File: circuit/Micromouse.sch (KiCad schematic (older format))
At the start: 33 parts, among them J1 DBG_CN, J3 TEST_1P, J5 TEST_1P, J6 Conn_01x04, Q2 IRLML6344, SW2 SW_Push, SW3 SW_Push, SW4 SW_Push, U3 STM32F405RGTx, U7 ICM-20602-module

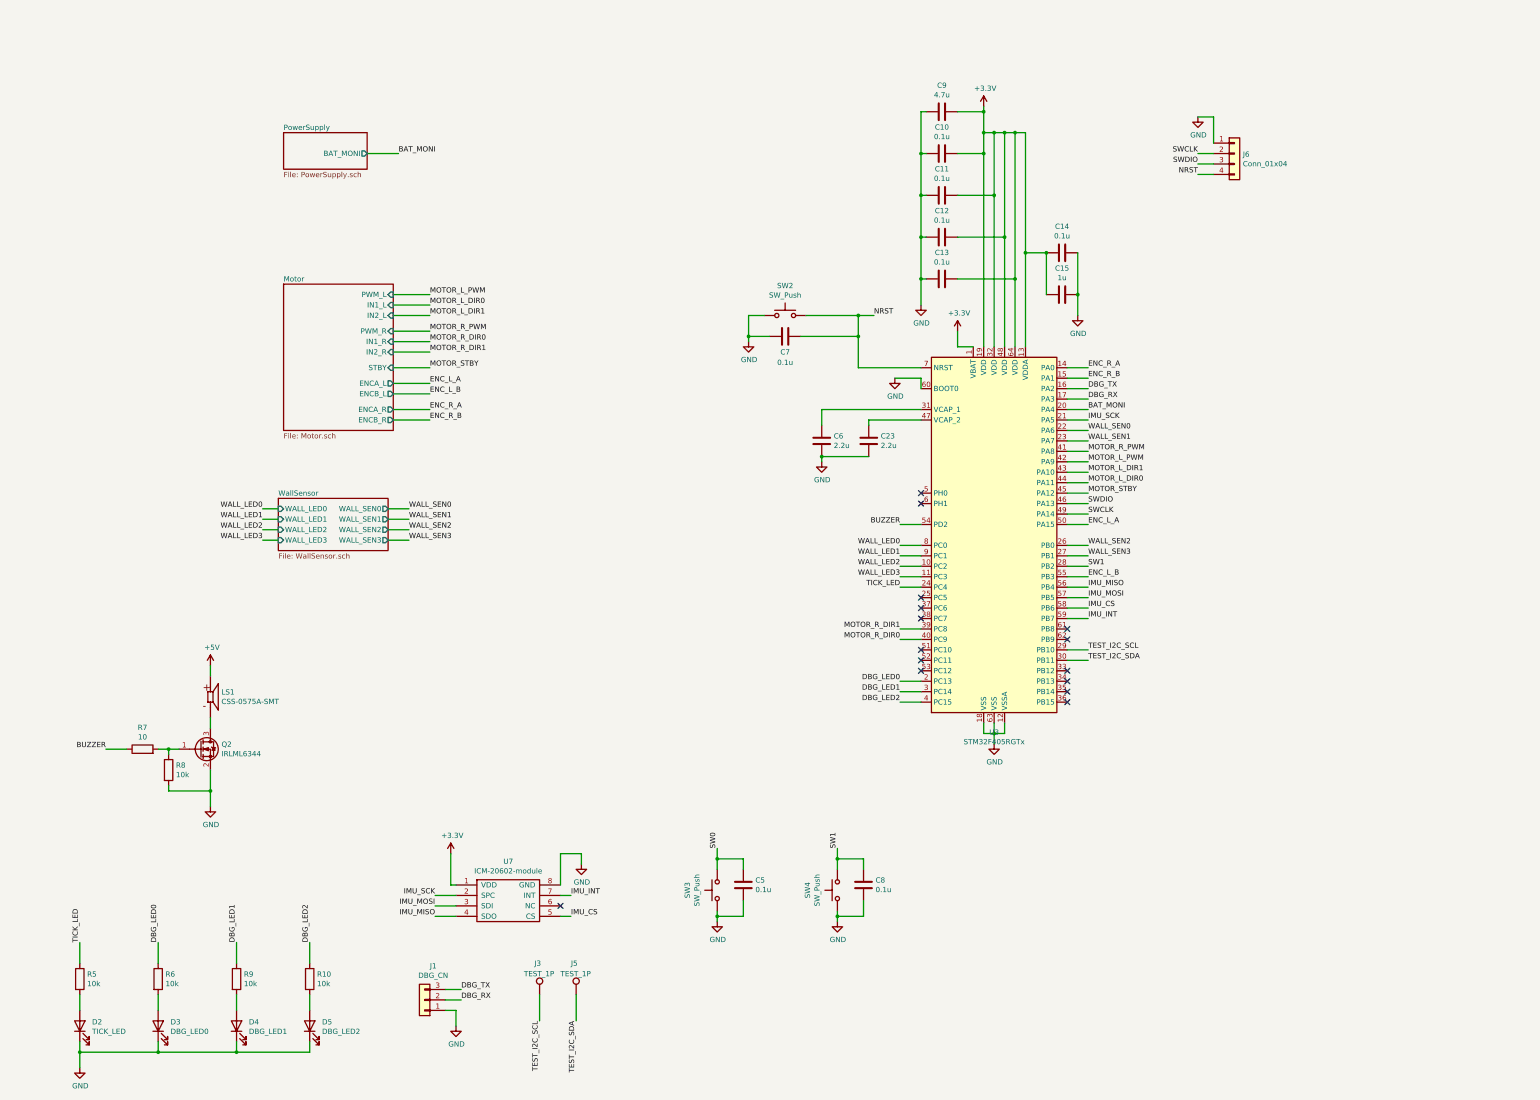
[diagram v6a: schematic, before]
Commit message: 残すはGNDビアとGND分離・・・
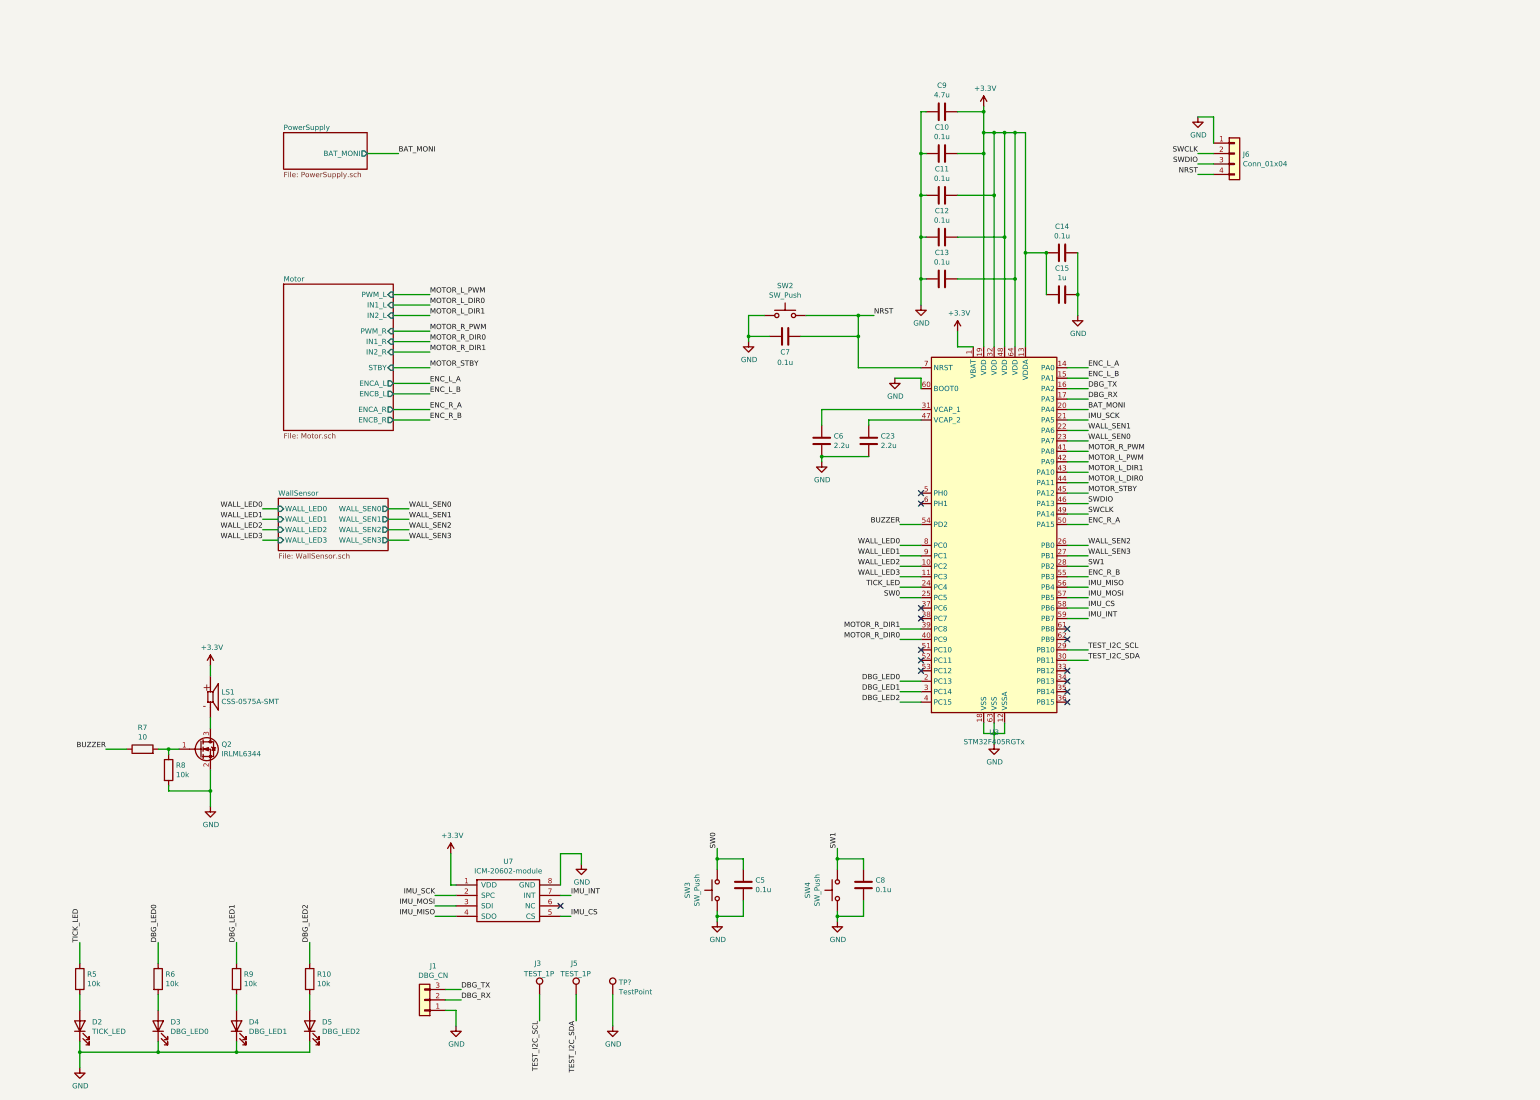
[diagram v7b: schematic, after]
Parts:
- added TP?: TestPoint, symbol Connector:TestPoint
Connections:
- net +5V is gone; now on net +3V3: LS1.1
- net ENC_L_A: now also U3.14 (PA0); no longer U3.50 (PA15)
- net ENC_L_B: now also U3.15 (PA1); no longer U3.55 (PB3)
- net ENC_R_A: now also U3.50 (PA15); no longer U3.14 (PA0)
- net ENC_R_B: now also U3.55 (PB3); no longer U3.15 (PA1)
- net GND: now also TP?.1
- net SW0: now also U3.25 (PC5)
- net WALL_SEN0: now also U3.23 (PA7); no longer U3.22 (PA6)
- net WALL_SEN1: now also U3.22 (PA6); no longer U3.23 (PA7)
- no-connect marks 15 -> 14
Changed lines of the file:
@@
 	10850 3800 11050 3800
 Text Label 11050 3900 0    50   ~ 0
-ENC_R_B
+ENC_L_B
 Wire Wire Line
 	10850 3900 11050 3900
 Text Label 11050 3800 0    50   ~ 0
-ENC_R_A
+ENC_L_A
 Text Label 11050 4000 0    50   ~ 0
 DBG_TX
@@
 	10850 4300 11050 4300
 Text Label 11050 4400 0    50   ~ 0
-WALL_SEN0
+WALL_SEN1
 Wire Wire Line
 	10850 4400 11050 4400
 Text Label 11050 4500 0    50   ~ 0
-WALL_SEN1
+WALL_SEN0
 Wire Wire Line
 	10850 4500 11050 4500
@@
 	10850 5000 11050 5000
 Text Label 11050 5300 0    50   ~ 0
-ENC_L_A
+ENC_R_A
 Wire Wire Line
 	10850 5300 11050 5300
 Text Label 11050 5800 0    50   ~ 0
-ENC_L_B
+ENC_R_B
 Wire Wire Line
 	10850 5800 11050 5800
@@
 NoConn ~ 10850 6400
 NoConn ~ 10850 6300
-NoConn ~ 9450 6000
 Text Label 7500 8400 1    50   ~ 0
 SW0
@@
 $EndComp
 $Comp
-L power:+5V #PWR0128
-U 1 1 5FAB5052
-P 2650 6650
-F 0 "#PWR0128" H 2650 6500 50  0001 C CNN
-F 1 "+5V" H 2665 6823 50  0000 C CNN
-F 2 "" H 2650 6650 50  0001 C CNN
-F 3 "" H 2650 6650 50  0001 C CNN
-	1    2650 6650
-	1    0    0    -1
-$EndComp
-$Comp
 L Connector_Generic:Conn_01x03 J1
 U 1 1 5FA91BF0
@@
 	6000 8850 6100 8850
 NoConn ~ 6000 8950
+$Comp
+L power:+3.3V #PWR0128
+U 1 1 5FCF8981
+P 2650 6650
+F 0 "#PWR0128" H 2650 6500 50  0001 C CNN
+F 1 "+3.3V" H 2665 6823 50  0000 C CNN
+F 2 "" H 2650 6650 50  0001 C CNN
+F 3 "" H 2650 6650 50  0001 C CNN
+	1    2650 6650
+	1    0    0    -1
+$EndComp
+Text Label 9250 6000 2    50   ~ 0
+SW0
+Wire Wire Line
+	9250 6000 9450 6000
+$Comp
+L Connector:TestPoint TP?
+U 1 1 5FFC074B
+P 6500 9800
+F 0 "TP?" H 6558 9918 50  0000 L CNN
+F 1 "TestPoint" H 6558 9827 50  0000 L CNN
+F 2 "" H 6700 9800 50  0001 C CNN
+F 3 "~" H 6700 9800 50  0001 C CNN
+	1    6500 9800
+	1    0    0    -1
+$EndComp
+$Comp
+L power:GND #PWR?
+U 1 1 5FFC282D
+P 6500 10100
+F 0 "#PWR?" H 6500 9850 50  0001 C CNN
+F 1 "GND" H 6505 9927 50  0000 C CNN
+F 2 "" H 6500 10100 50  0001 C CNN
+F 3 "" H 6500 10100 50  0001 C CNN
+	1    6500 10100
+	1    0    0    -1
+$EndComp
+Wire Wire Line
+	6500 9800 6500 10100
 $EndSCHEMATC

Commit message: AW終わったああああああああああああああ（はず）
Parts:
- TP1: renamed from TP?; footprint (none) -> TestPoint:TestPoint_Pad_D1.0mm
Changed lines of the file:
@@
 	9250 6000 9450 6000
 $Comp
-L Connector:TestPoint TP?
+L Connector:TestPoint TP1
 U 1 1 5FFC074B
 P 6500 9800
-F 0 "TP?" H 6558 9918 50  0000 L CNN
+F 0 "TP1" H 6558 9918 50  0000 L CNN
 F 1 "TestPoint" H 6558 9827 50  0000 L CNN
-F 2 "" H 6700 9800 50  0001 C CNN
+F 2 "TestPoint:TestPoint_Pad_D1.0mm" H 6700 9800 50  0001 C CNN
 F 3 "~" H 6700 9800 50  0001 C CNN
 	1    6500 9800
@@
 $EndComp
 $Comp
-L power:GND #PWR?
+L power:GND #PWR0149
 U 1 1 5FFC282D
 P 6500 10100
-F 0 "#PWR?" H 6500 9850 50  0001 C CNN
+F 0 "#PWR0149" H 6500 9850 50  0001 C CNN
 F 1 "GND" H 6505 9927 50  0000 C CNN
 F 2 "" H 6500 10100 50  0001 C CNN
